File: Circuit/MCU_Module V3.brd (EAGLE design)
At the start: 160 x 100 mm, 44 parts, among them IC1 75176BD, Q1 8MHZ, T1 BC848, T2 BC848

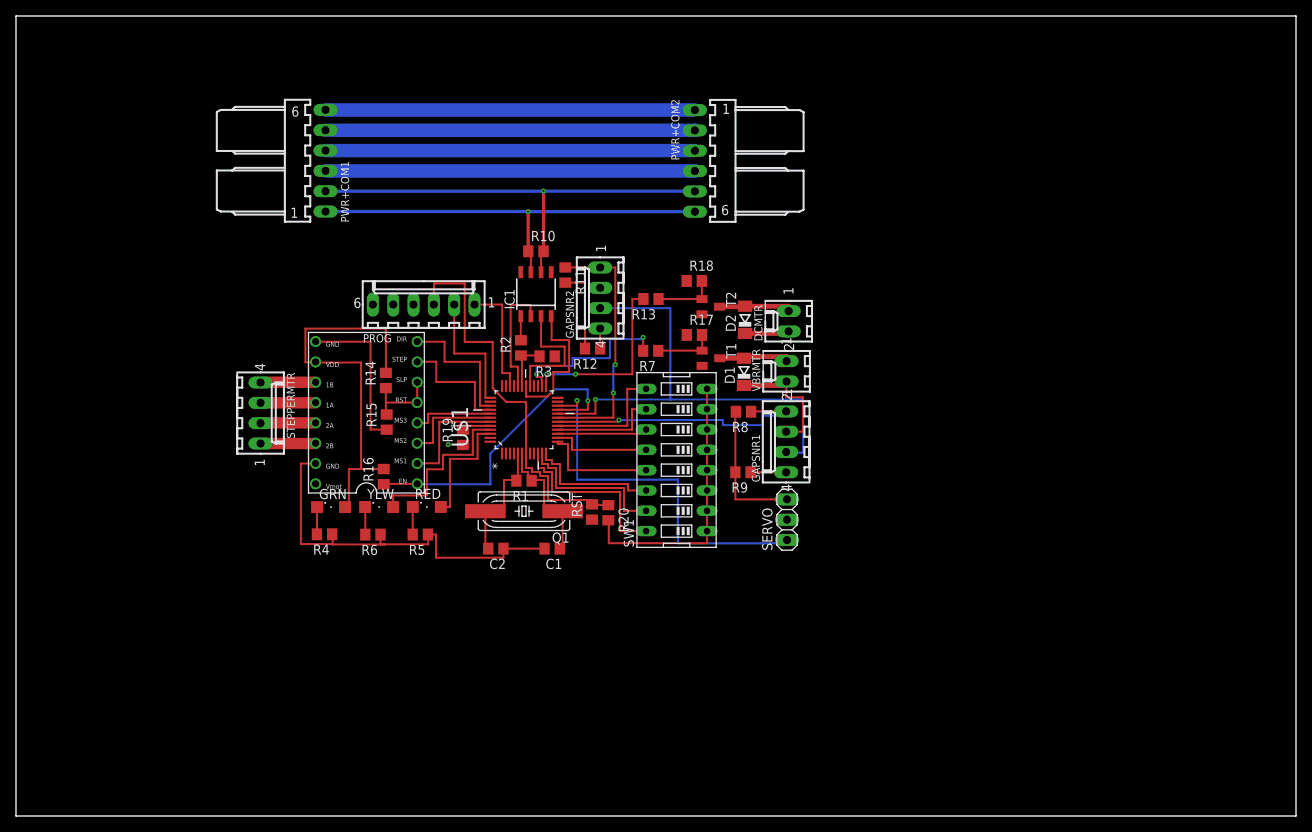
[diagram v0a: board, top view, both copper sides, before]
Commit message: redid layout and updated document
updated the document and redid the layout to improve layout and added
more initilizaton to the document
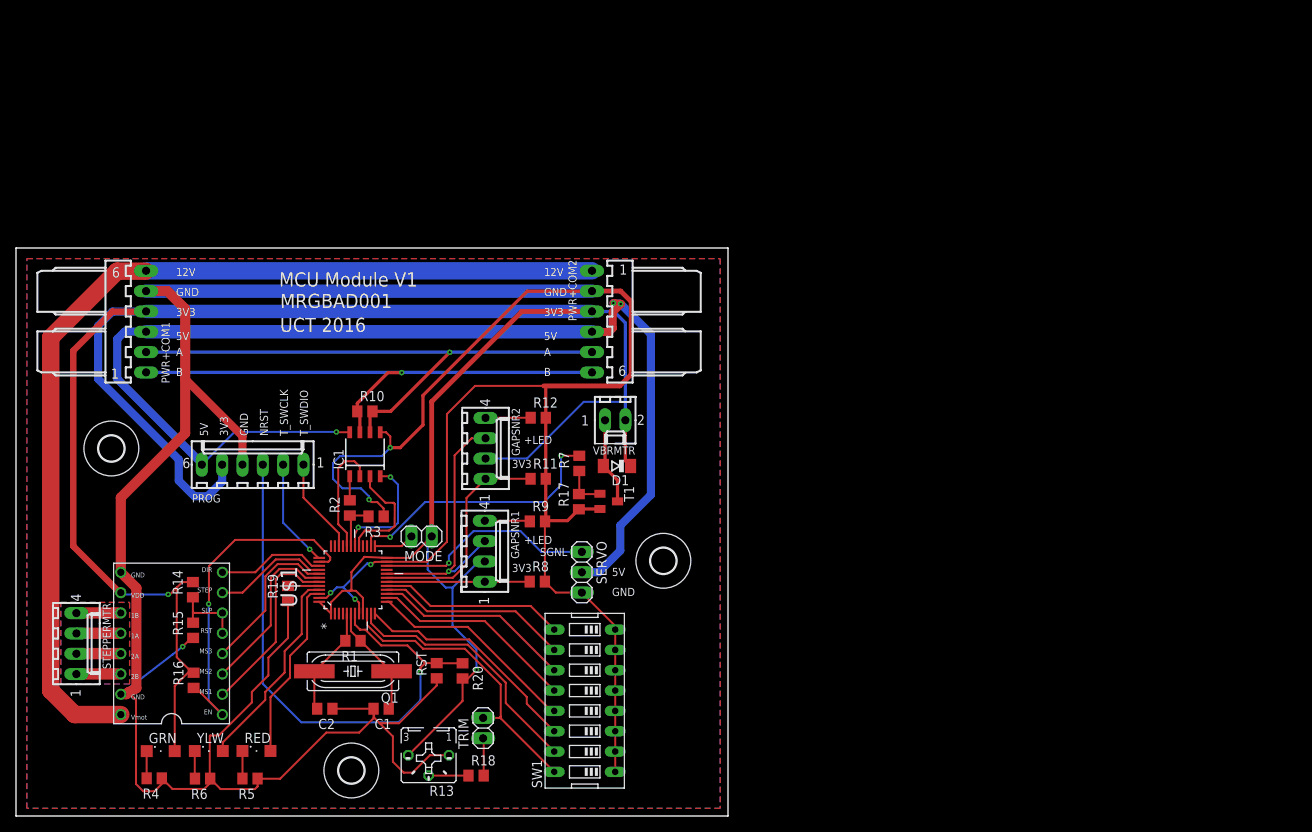
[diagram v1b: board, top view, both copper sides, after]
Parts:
- removed D2: LL4148, diode:SOD80C
- removed DCMTR: DCMOTOR, con-molex:6410-02
- removed T2: BC848, transistor:SOT23
- added MODE, TRIM: (no value), pinhead:1X02
- added U$3, U$4, U$5: (no value), holes:3,2
- R13: value 120 -> 5k; device rcl:R0805 -> pot:B25P
- R18: value 10k -> 2k; device rcl:R0805 -> resistor:R0805
- moved R18 67.6 mm to (57.5, 5.05)
- moved R13 63.4 mm to (51.6, 7.60)
- moved GAPSNR1 40.1 mm to (58.6, 33.1), turned to 270 degrees
- moved U$2 37.7 mm to (14.4, 13.9)
- moved GRN 37.2 mm to (18.1, 8.11)
- moved R4 37.2 mm to (17.3, 4.71)
- moved R5 37.2 mm to (29.2, 4.68)
- moved R6 37.2 mm to (23.3, 4.67)
- moved RED 37.2 mm to (30.1, 8.13)
- moved YLW 37.2 mm to (24.1, 8.12)
- moved STEPPERMTR 36.9 mm to (7.55, 21.6)
- moved R14 35.6 mm to (22.1, 28.3)
- moved R15 35.5 mm to (22.1, 23.2)
- moved R16 34.8 mm to (22.2, 17.0)
- moved R8 33.4 mm to (65.2, 29.3), turned to 0 degrees
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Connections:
- net N$13 renamed 8IN
- removed net DCMTR: R13.2, U$1.25
- removed net MTR2-: D2.A, DCMTR.1, T2.3
- removed net N$3: SW1.16, U$1.10
- removed net N$4: R13.1, R18.2, T2.1
- new net 1IN: SW1.16, TRIM.2, U$1.10
- new net MODE: MODE.2, U$1.25
- new net N$13: R13.S, R18.1
- new net N$23: R18.2, TRIM.1
- net 3V3: now also MODE.1, R13.E; no longer SW1.1, SW1.2, SW1.3, SW1.4, SW1.5, SW1.6, SW1.7, SW1.8
- net 5V: no longer D2.C, DCMTR.2
- net EN: now also U$1.38; no longer U$1.21
- net GND: now also R13.A, SW1.1, SW1.2, SW1.3, SW1.4, SW1.5, SW1.6, SW1.7, SW1.8; no longer R18.1, T2.2
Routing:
- net GND: track 145.0 -> 446.2 mm, vias 0 -> 6
- net 3V3: track 146.7 -> 320.9 mm, vias 0 -> 2
- net 5V: track 51.9 -> 148.1 mm, vias 0 -> 3
- net 12V: track 46.2 -> 125.2 mm
- net 1IN: track 0.00 -> 37.2 mm
- net IRLED: track 61.5 -> 33.5 mm
- net N$3: track 23.2 -> 0.00 mm
- net DCMTR: track 23.1 -> 0.00 mm, vias 2 -> 0
- net NRST: track 51.2 -> 72.0 mm, vias 0 -> 1
- net SGNL: track 47.6 -> 27.8 mm
- net VSENSE1: track 35.0 -> 17.9 mm, vias 1 -> 0
- net A: track 56.7 -> 71.2 mm
- net N$11: track 11.6 -> 24.9 mm
- net N$10: track 12.5 -> 25.7 mm
- net B: track 54.1 -> 66.7 mm
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- added copper zone on layer 1, net GND
- added copper zone on layer 16, net GND
- added copper zone on layer 16, net N$28
- added copper zone on layer 1, net N$3
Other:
- board size 160 x 100 mm -> 89 x 71 mm
- board text added: "+LED"
- board text added: "12V"
- board text added: "3V3"
- board text added: "5V"
- board text added: "A"
- board text added: "B"
- board text added: "GND"
- board text added: "MCU Module V1"
- board text added: "MRGBAD001"
- board text added: "NRST"
- board text added: "SGNL"
- board text added: "T_SWCLK"
- board text added: "T_SWDIO"
- board text added: "UCT 2016"
